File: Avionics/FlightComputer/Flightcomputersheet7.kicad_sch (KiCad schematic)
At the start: 22 parts

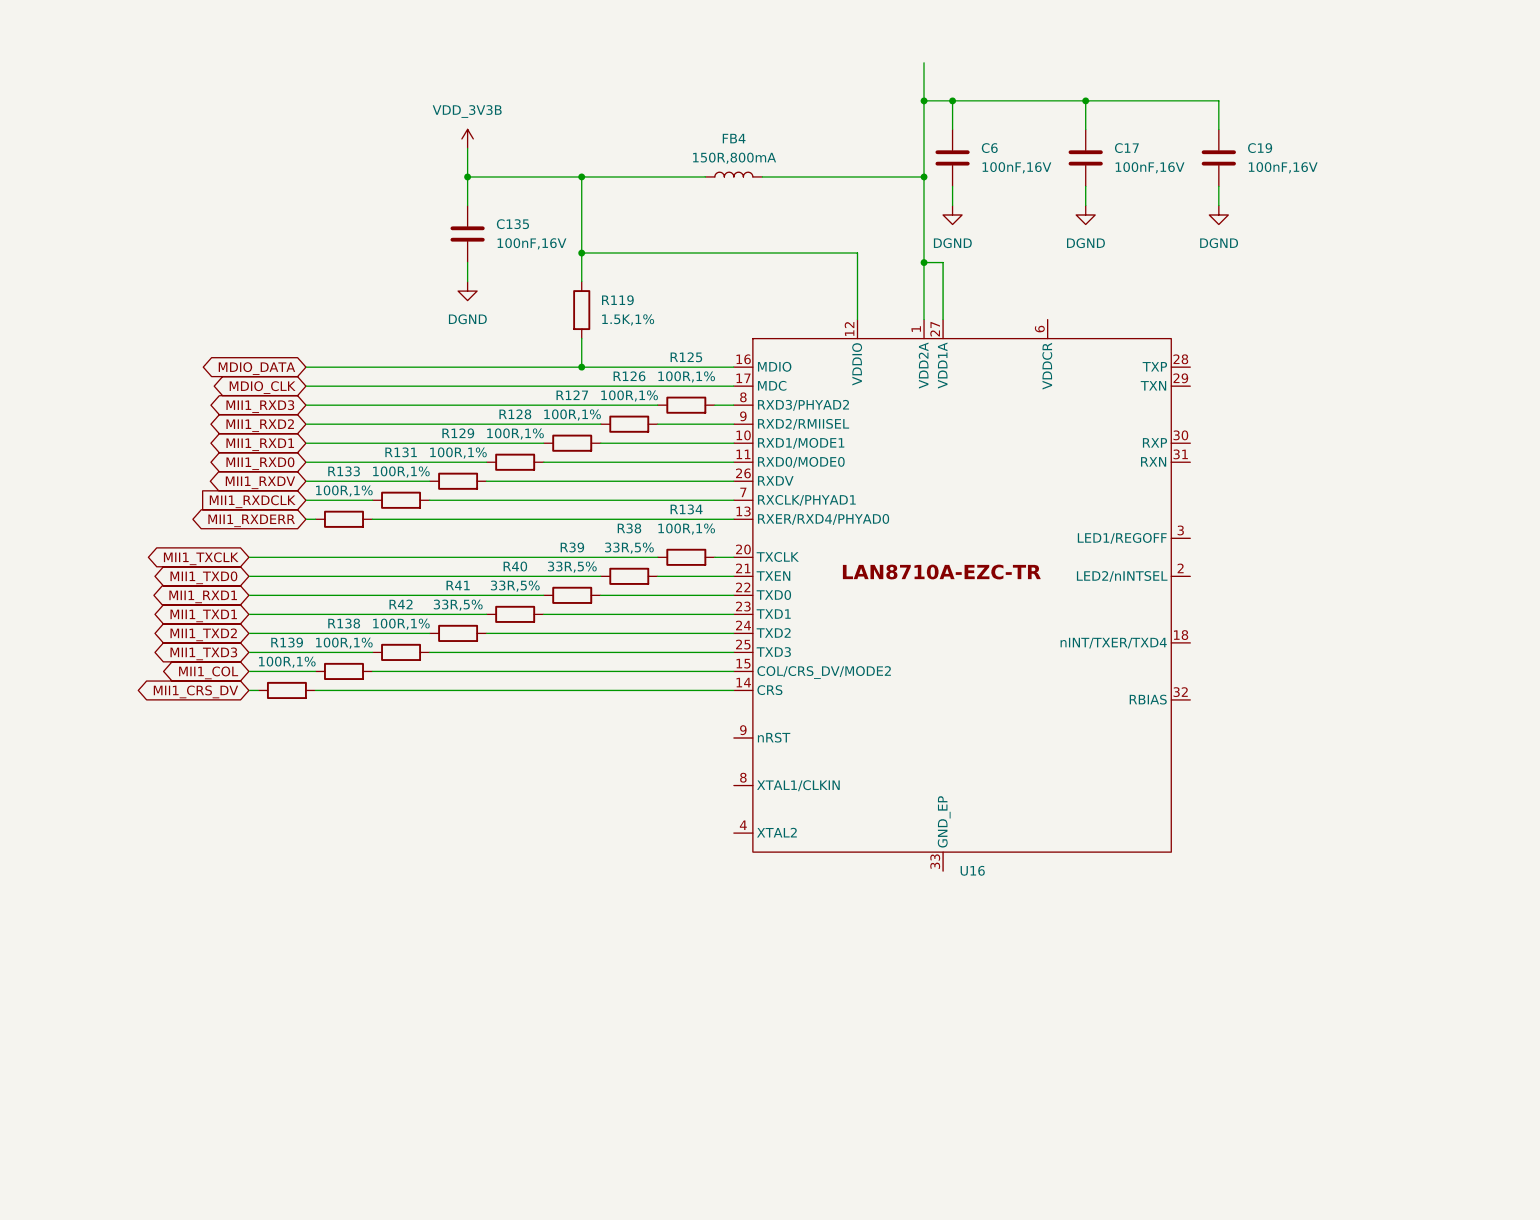
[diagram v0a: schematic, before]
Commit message: Ian Goldberg - Created a motherboard for the BeagleBone to alow ot to be mounted in the PC104 stack
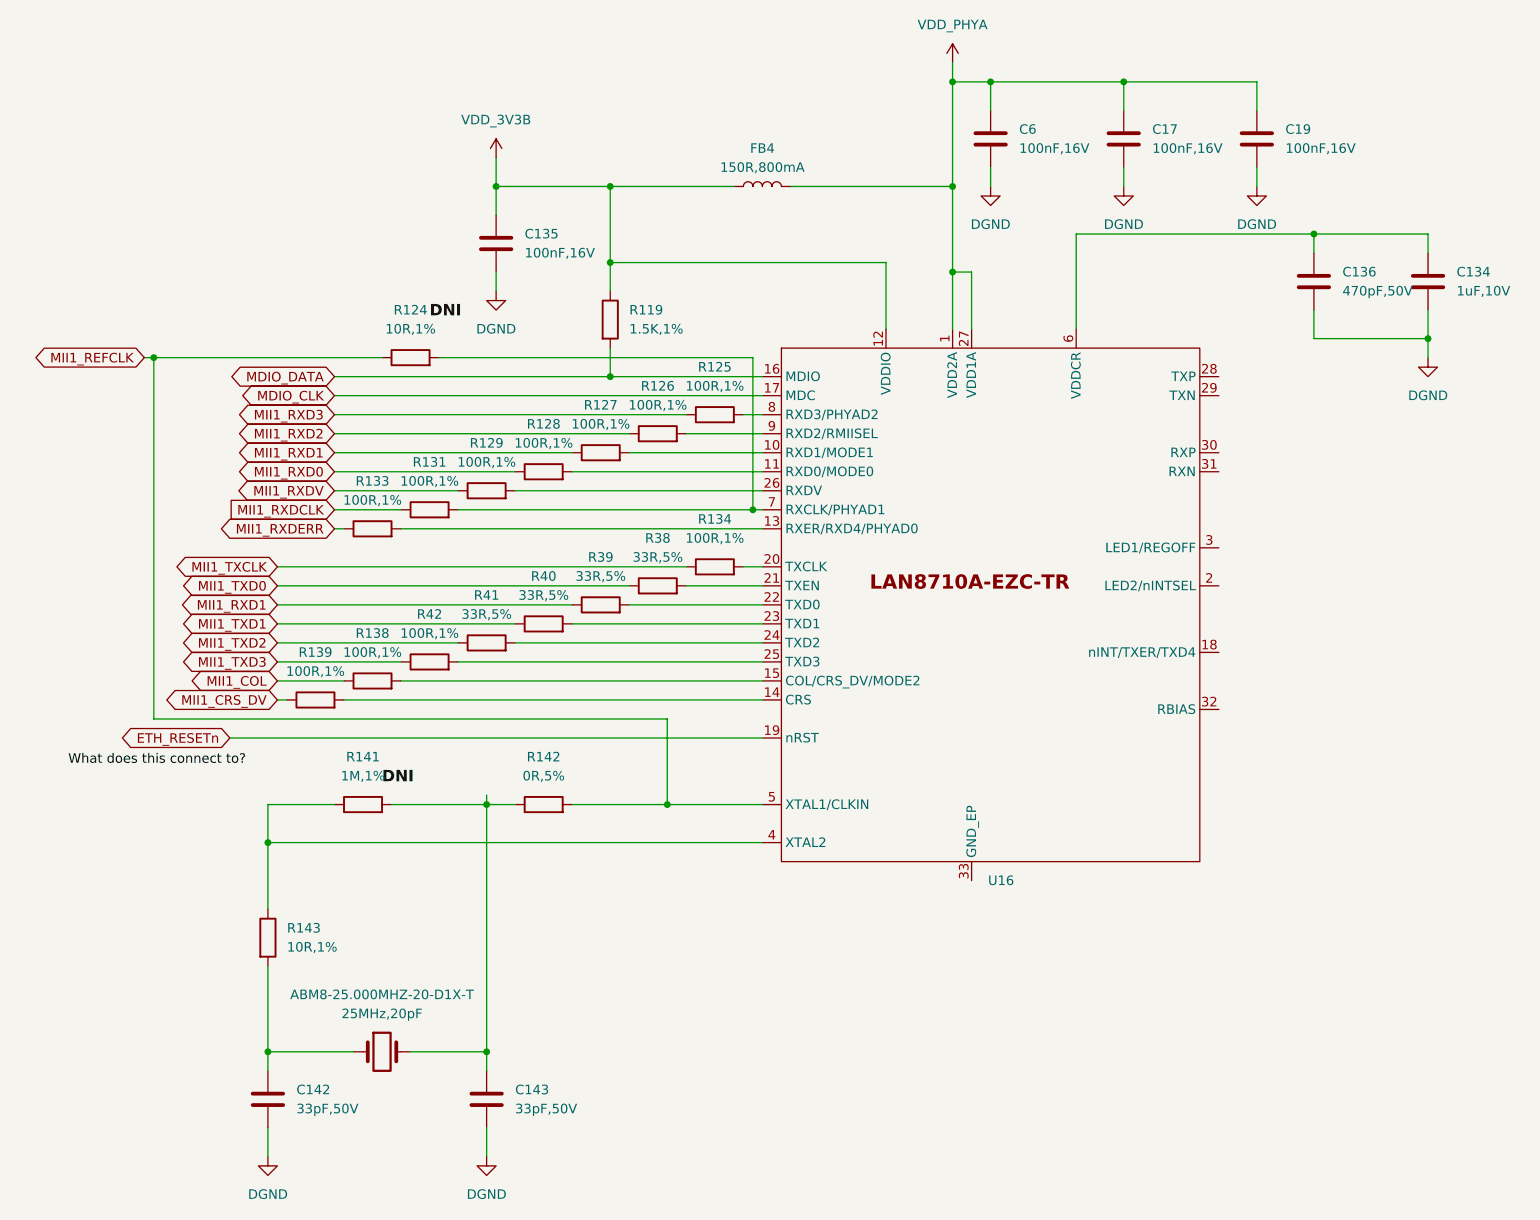
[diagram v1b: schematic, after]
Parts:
- added ABM8-25.000MHZ-20-D1X-T: 25MHz,20pF, symbol Device:Crystal
- added C134: 1uF,10V, symbol Device:C
- added C136: 470pF,50V, symbol Device:C
- added C142, C143: 33pF,50V, symbol Device:C
- added R124, R143: 10R,1%, symbol Device:R
- added R141: 1M,1%, symbol Device:R
- added R142: 0R,5%, symbol Device:R
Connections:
- net DGND: now also C134.2, C136.2, C142.2, C143.2
- net at R131.2, U16.7 (RXCLK/PHYAD1): now also R124.2
- net VDD_PHYA: now reaches C17.1, C19.1, C6.1, FB4.2, U16.1 (VDD2A), U16.27 (VDD1A)
- net at U16.4 (XTAL2): now also R141.1, R143.1
- net at U16.6 (VDDCR): now also C134.1, C136.1
- net at U16.8 (RXD3/PHYAD2): now also R125.2
- new net: ABM8-25.000MHZ-20-D1X-T.1, C142.1, R143.2
- new net: ABM8-25.000MHZ-20-D1X-T.2, C143.1, R141.2, R142.1
- new net ETH_RESETn: U16.19 (nRST)
- new net MII1_REFCLK: R124.1, R142.2, U16.5 (XTAL1/CLKIN)
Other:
- moved on the sheet: C135, C17, C19, C6, FB4, R119, R125, R126, R127, R128, R129, R131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
